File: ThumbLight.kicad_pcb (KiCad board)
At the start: 2 copper layers, 23.5 x 43.8 mm, 6 parts, among them J1 USB_A, U1 DHT11, U2 UA78M33_TO252, U3 ESP-12E, U4 TTL

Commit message: New basic layout
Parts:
- JP1: footprint Connector_PinHeader_2.54mm:PinHeader_1x02_P2.54mm_Vertical -> Connector_PinHeader_2.54mm:PinHeader_1x03_P2.54mm_Vertical
- moved U3 87.0 mm to (100.0, 116.0), turned to 0 degrees
- moved U2 85.2 mm to (94.0, 85.0)
- moved J1 84.4 mm to (100.0, 72.0)
- moved U1 82.9 mm to (113.0, 93.1), turned to 180 degrees
- moved JP1 76.9 mm to (110.3, 102.8), turned to 180 degrees
- moved U4 68.5 mm to (112.3, 119.9), turned to 180 degrees
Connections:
- U3 pad 19: unconnected-(U3-Pad19) -> TEMP
- U3 pad 7: TEMP -> unconnected-(U3-Pad7)
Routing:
- net TEMP: track 7.78 -> 32.7 mm
- net +3V3: track 60.4 -> 74.8 mm
- net +5V: track 7.63 -> 13.2 mm
- net GND: track 8.30 -> 9.88 mm
- net RX: track 6.61 -> 5.81 mm
- net TX: track 6.39 -> 5.59 mm
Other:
- board size 23.5 x 43.8 mm -> 32 x 49 mm

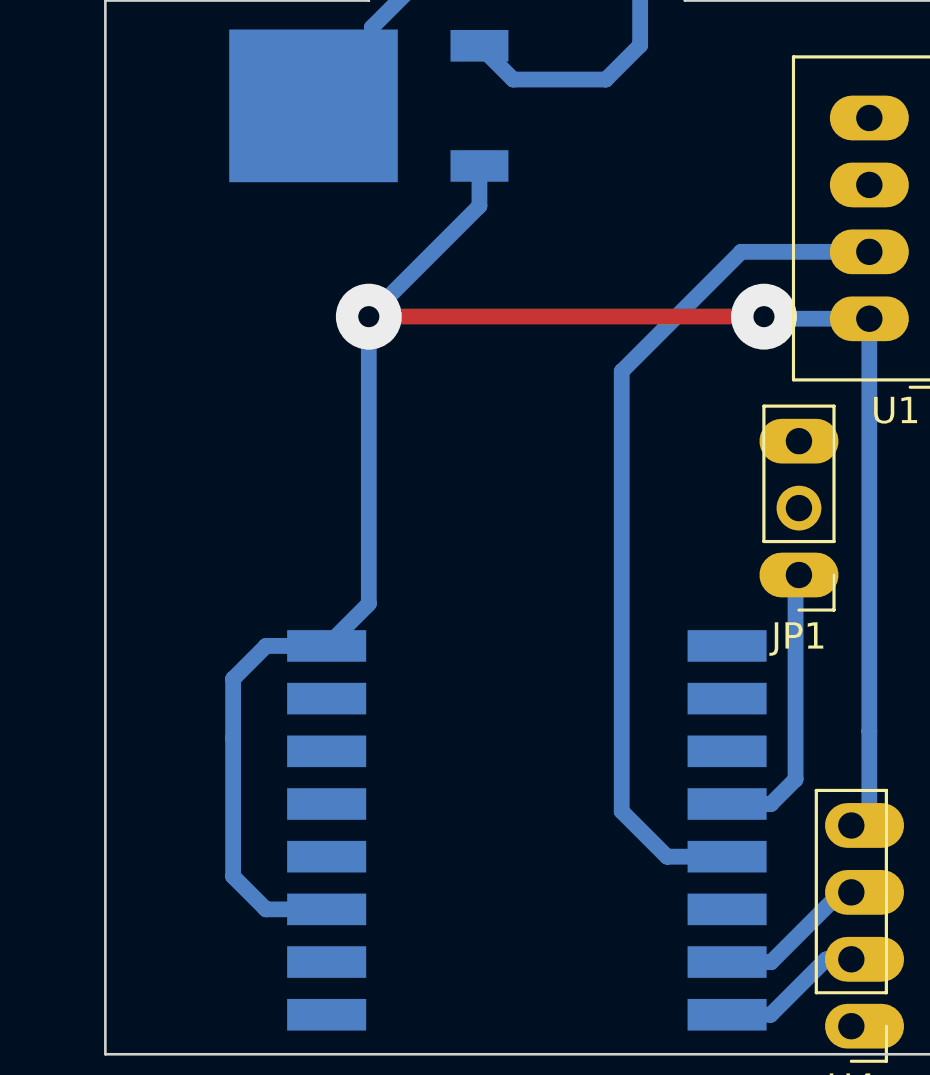
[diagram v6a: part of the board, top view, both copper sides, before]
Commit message: Add neopixel strip
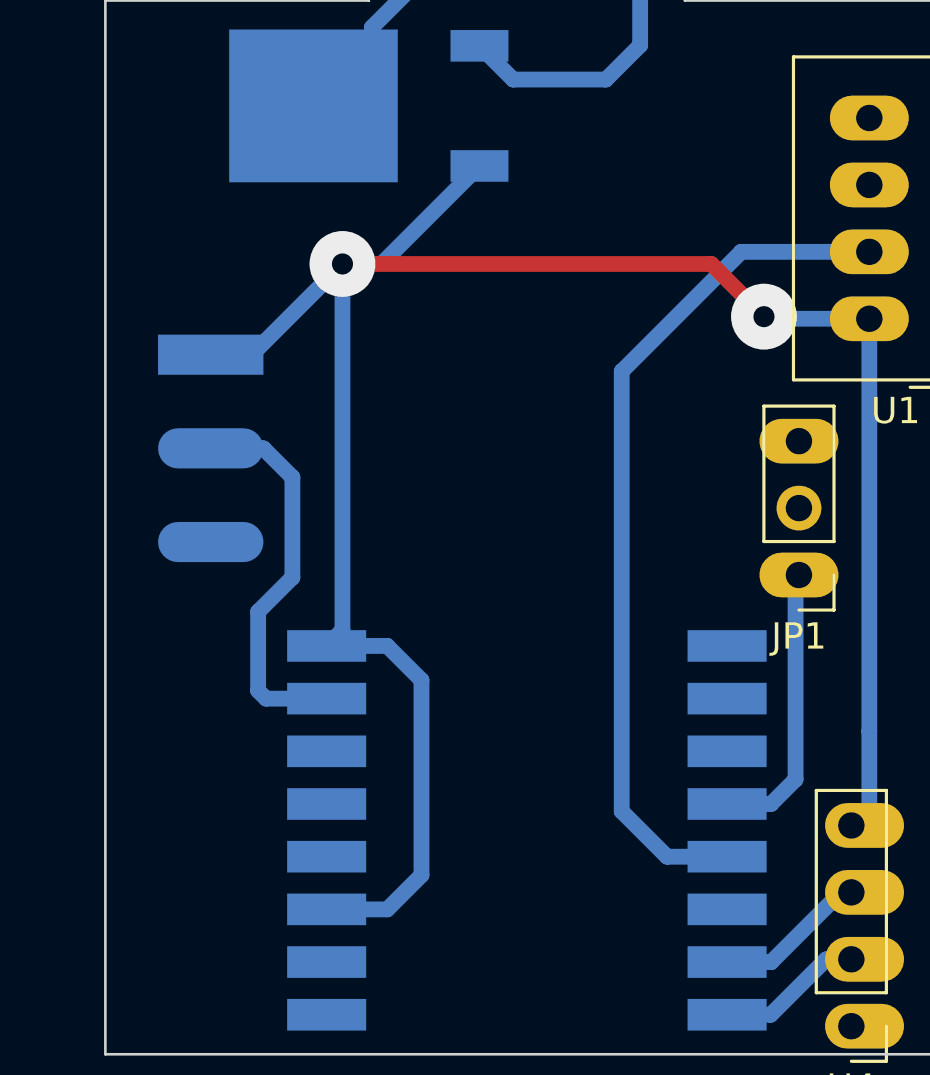
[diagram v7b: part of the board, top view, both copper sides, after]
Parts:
- added LIN1: LEDs_In, neopixel-strip:neopixel-strip, B.Cu at (88.0, 98.0)
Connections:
- U3 pad 7: unconnected-(U3-Pad7) -> NEOPIXEL
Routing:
- net NEOPIXEL: track 0.00 -> 14.9 mm
- net +3V3: track 74.8 -> 84.0 mm

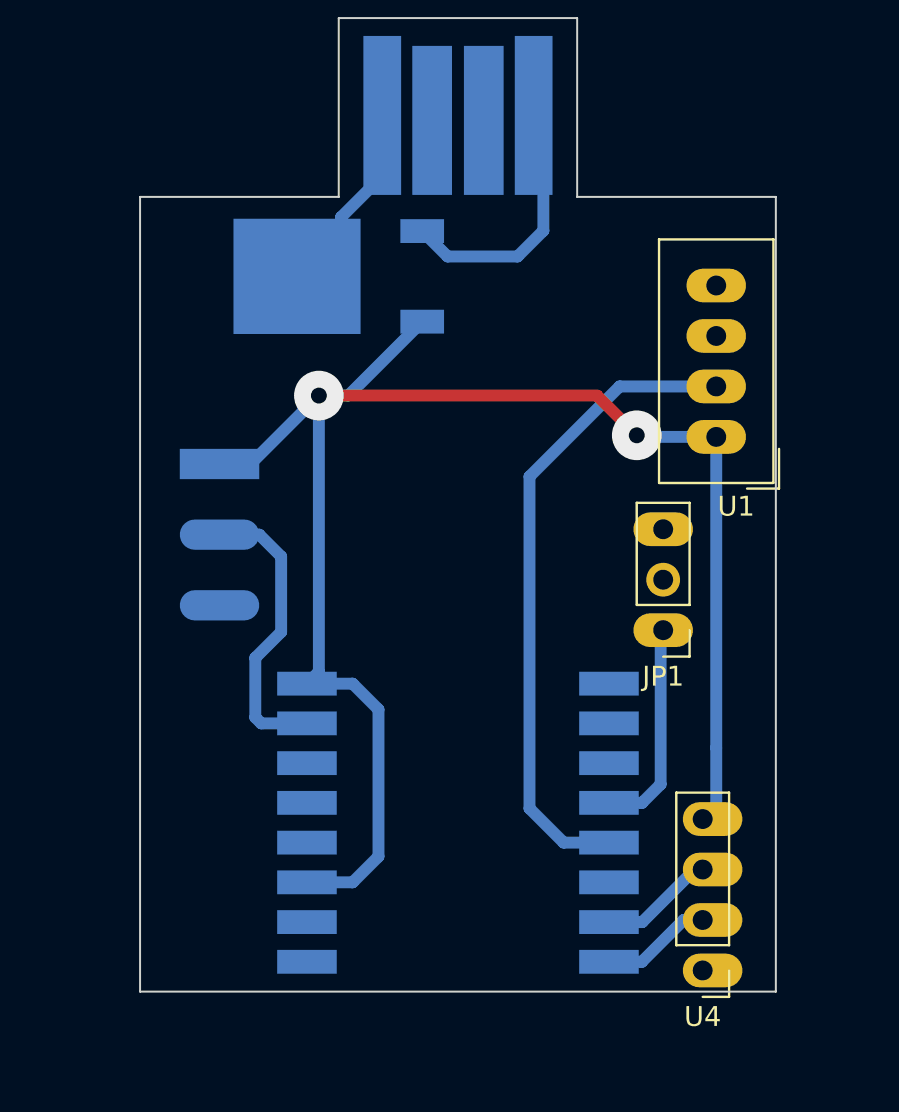
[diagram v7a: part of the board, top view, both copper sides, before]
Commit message: Add buttons and light sensor
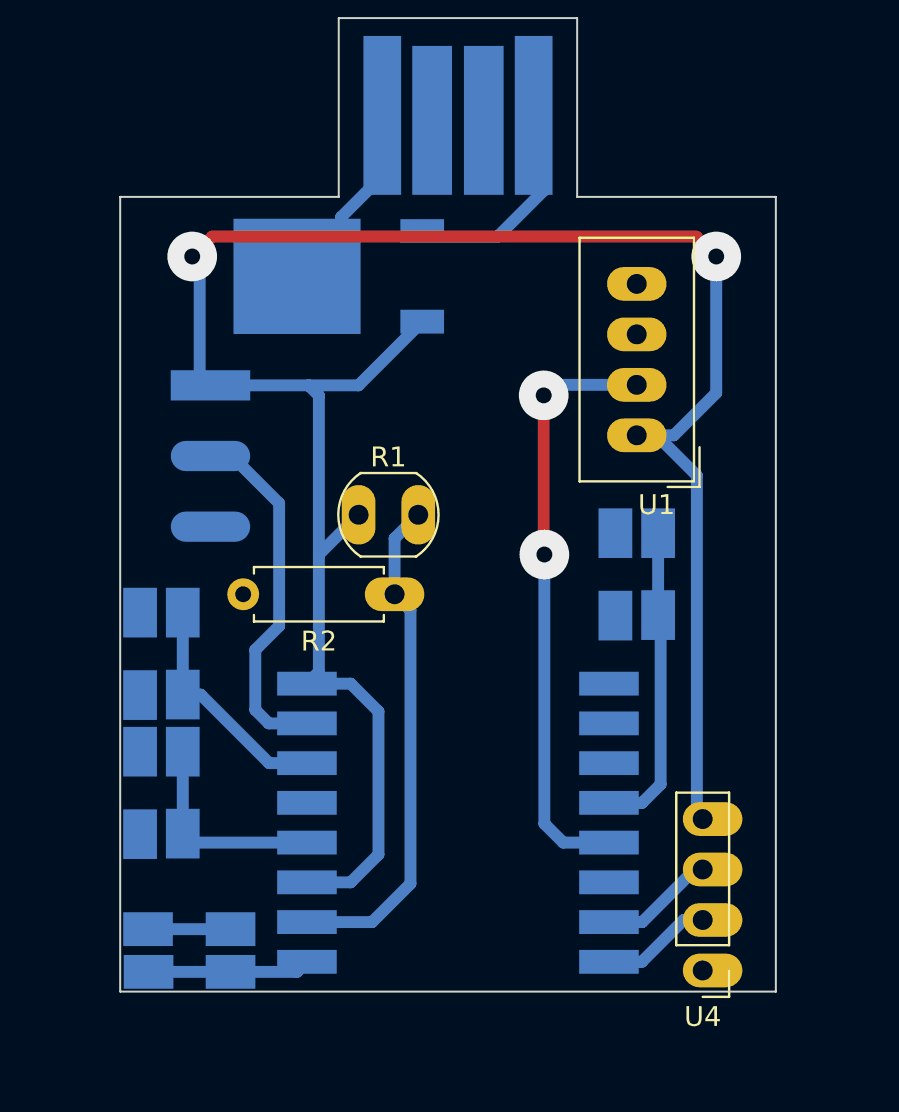
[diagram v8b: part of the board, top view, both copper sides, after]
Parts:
- removed JP1: PROG, Connector_PinHeader_2.54mm:PinHeader_1x03_P2.54mm_Vertical
- added R1: R_Photo, OptoDevice:R_LDR_5.0x4.1mm_P3mm_Vertical, F.Cu at (95.0, 97.0)
- added R2: 10k, Resistor_THT:R_Axial_DIN0207_L6.3mm_D2.5mm_P7.62mm_Horizontal, F.Cu at (96.8, 101.0)
- added SW1: RESET, Button_Switch_SMD:SW_Push_1P1T_NO_Vertical_Wuerth_434133025816, B.Cu at (86.5, 118.9)
- added SW2: RESET, Button_Switch_SMD:SW_Push_1P1T_NO_Vertical_Wuerth_434133025816, B.Cu at (85.1, 111.0)
- added SW3: RESET, Button_Switch_SMD:SW_Push_1P1T_NO_Vertical_Wuerth_434133025816, B.Cu at (85.1, 104.0)
- added SW4: RESET, Button_Switch_SMD:SW_Push_1P1T_NO_Vertical_Wuerth_434133025816, B.Cu at (109.0, 100.0)
- moved U1 4.00 mm to (109.0, 93.0)
- moved LIN1 3.98 mm to (87.5, 94.0)
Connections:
- U3 pad 1: unconnected-(U3-Pad1) -> Net-(SW1-Pad2)
- U3 pad 2: unconnected-(U3-Pad2) -> Net-(U3-Pad2)
- U3 pad 4: unconnected-(U3-Pad4) -> BUTTON-A
- U3 pad 6: unconnected-(U3-Pad6) -> BUTTON-B
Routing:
- net +3V3: track 84.0 -> 112.9 mm
- net Net-(U3-Pad2): track 0.00 -> 25.4 mm
- net BUTTON-B: track 0.00 -> 11.8 mm
- net BUTTON-A: track 0.00 -> 10.6 mm
- net Net-(SW1-Pad2): track 0.00 -> 8.18 mm
- net GND: track 9.88 -> 14.0 mm
- net Net-(SW4-Pad2): track 10.8 -> 14.9 mm
- net NEOPIXEL: track 14.9 -> 18.2 mm
- net TEMP: track 32.7 -> 30.1 mm, vias 0 -> 2
- net +5V: track 13.2 -> 11.2 mm
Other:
- board size 32 x 49 mm -> 33 x 49 mm
